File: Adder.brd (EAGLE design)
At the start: 100 x 50 mm, 57 parts, among them U1 LMS8117

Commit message: Updated a few traces
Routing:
- net 3.3V: track 167.7 -> 165.4 mm
- net GND: vias 24 -> 30
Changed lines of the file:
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@@
 <wire x1="2.5" y1="2.25" x2="4" y2="2.25" width="0.1524" layer="1"/>
 <wire x1="1.75" y1="3" x2="2.5" y2="2.25" width="0.1524" layer="1"/>
-<wire x1="1.75" y1="24.25" x2="1.75" y2="10.75" width="0.1524" layer="1"/>
 <wire x1="1.75" y1="10.75" x2="1.75" y2="3" width="0.1524" layer="1"/>
-<wire x1="3.25" y1="24.25" x2="1.75" y2="24.25" width="0.1524" layer="1"/>
 <wire x1="4.75" y1="3" x2="4.95" y2="3" width="0.1524" layer="1"/>
 <wire x1="3.25" y1="24.25" x2="3.225" y2="24.225" width="0.1524" layer="1"/>
@@
 <wire x1="2" y1="11" x2="3.75" y2="11" width="0.1524" layer="16"/>
 <wire x1="2" y1="10.75" x2="2" y2="11" width="0.1524" layer="16"/>
-<wire x1="1.75" y1="10.75" x2="2" y2="10.75" width="0.1524" layer="1"/>
+<wire x1="2" y1="10.75" x2="1.75" y2="10.75" width="0.1524" layer="1"/>
 <wire x1="4.75" y1="12" x2="4.95" y2="12" width="0.1524" layer="1"/>
 <wire x1="84.25" y1="25" x2="84.25" y2="15" width="0.1524" layer="1"/>
@@
 <via x="85.5" y="9.5" extent="1-16" drill="0.35"/>
 <via x="18.5" y="47" extent="1-16" drill="0.35"/>
+<wire x1="3.225" y1="24.225" x2="2.225" y2="24.225" width="0.1524" layer="1"/>
+<wire x1="1.5" y1="23.5" x2="1.5" y2="11.25" width="0.1524" layer="1"/>
+<wire x1="1.5" y1="11.25" x2="2" y2="10.75" width="0.1524" layer="1"/>
+<wire x1="2.225" y1="24.225" x2="1.5" y2="23.5" width="0.1524" layer="1"/>
+<via x="9.5" y="17" extent="1-16" drill="0.35"/>
+<via x="32" y="12.5" extent="1-16" drill="0.35"/>
+<via x="34.5" y="17" extent="1-16" drill="0.35"/>
+<via x="34.5" y="25" extent="1-16" drill="0.35"/>
+<via x="25.5" y="5" extent="1-16" drill="0.35"/>
+<via x="41.5" y="36.5" extent="1-16" drill="0.35"/>
 </signal>
 <signal name="3.3V">
@@
 <wire x1="7.00921875" y1="44.85" x2="7.37" y2="44.85" width="0.6096" layer="1"/>
 <wire x1="7.37" y1="44.85" x2="9.3" y2="46.78" width="0.6096" layer="1"/>
-<wire x1="9.3" y1="42.55921875" x2="9.3" y2="40.48" width="0.6096" layer="1"/>
+<wire x1="9.3" y1="40.607309375" x2="9.3" y2="42.55921875" width="0.6096" layer="1"/>
+<wire x1="9.3" y1="40.607309375" x2="9.3" y2="40.48" width="0.6096" layer="1"/>
 <wire x1="9.3" y1="42.55921875" x2="7.00921875" y2="44.85" width="0.6096" layer="1"/>
 <wire x1="9.3" y1="40.48" x2="9.3" y2="39.7" width="0.6096" layer="1"/>
@@
 <wire x1="63.81" y1="18.54" x2="63.81" y2="16" width="0.6096" layer="1"/>
 <wire x1="63.81" y1="16" x2="63.81" y2="13.46" width="0.6096" layer="1"/>
-<wire x1="3.13" y1="27.9" x2="7.9" y2="27.9" width="0.2" layer="1"/>
+<wire x1="7.9" y1="27.9" x2="3.13" y2="27.9" width="0.2" layer="1"/>
 <wire x1="7.9" y1="27.9" x2="11" y2="31" width="0.2" layer="1"/>
 <wire x1="11" y1="31" x2="12.255" y2="31" width="0.2" layer="1"/>
 <wire x1="12.255" y1="31" x2="12.35" y2="31.095" width="0.2" layer="1"/>
-<wire x1="3.25" y1="39.25" x2="3.25" y2="28" width="0.1524" layer="1"/>
-<wire x1="9.5" y1="39.25" x2="3.25" y2="39.25" width="0.1524" layer="1"/>
 <wire x1="3.25" y1="28" x2="3.13" y2="27.9" width="0.1524" layer="1"/>
 <wire x1="9.5" y1="39.25" x2="9.625" y2="39.375" width="0.1524" layer="1"/>
@@
 <wire x1="36.4124625" y1="6.5" x2="37" y2="7.0875375" width="0.254" layer="1"/>
 <wire x1="28.6" y1="6.5" x2="36.4124625" y2="6.5" width="0.254" layer="1"/>
+<wire x1="3.13" y1="27.9" x2="3.13" y2="34.437309375" width="0.1524" layer="1"/>
+<wire x1="3.13" y1="34.437309375" x2="9.3" y2="40.607309375" width="0.1524" layer="1"/>
 </signal>
 <signal name="N$11">
@@
 <contactref element="R13" pad="2"/>
 <wire x1="29.25" y1="46" x2="28.25" y2="45" width="0.1524" layer="1"/>
-<wire x1="36" y1="46" x2="29.25" y2="46" width="0.1524" layer="1"/>
-<wire x1="37" y1="45" x2="36.5" y2="45.5" width="0.1524" layer="1"/>
-<wire x1="36.5" y1="45.5" x2="36" y2="46" width="0.1524" layer="1"/>
+<wire x1="29.25" y1="46" x2="36" y2="46" width="0.1524" layer="1"/>
+<wire x1="37" y1="45" x2="36" y2="46" width="0.1524" layer="1"/>
 <wire x1="28.25" y1="45" x2="28.1" y2="45" width="0.1524" layer="1"/>
 <wire x1="37" y1="45" x2="37.1" y2="45" width="0.1524" layer="1"/>
 <wire x1="43.5" y1="46.5" x2="44.25" y2="45.75" width="0.1524" layer="1"/>
 <wire x1="44.25" y1="45.75" x2="45" y2="45" width="0.1524" layer="1"/>
-<wire x1="37.5" y1="46.5" x2="43.5" y2="46.5" width="0.1524" layer="1"/>
-<wire x1="36.5" y1="45.5" x2="37.5" y2="46.5" width="0.1524" layer="1"/>
 <wire x1="45" y1="45" x2="45.1" y2="45" width="0.1524" layer="1"/>
 <wire x1="44" y1="43.25" x2="56" y2="31.25" width="0.1524" layer="16"/>
@@
 <wire x1="56" y1="31.25" x2="56.19" y2="31.24" width="0.1524" layer="16"/>
 <via x="44" y="45.5" extent="1-16" drill="0.35"/>
+<wire x1="36" y1="46" x2="36.5" y2="46.5" width="0.1524" layer="1"/>
+<wire x1="36.5" y1="46.5" x2="43.5" y2="46.5" width="0.1524" layer="1"/>
 </signal>
 <signal name="B0_IN">

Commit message: Made updates for v2
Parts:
- removed R19, R20, R21, R22: 51, SparkFun-Resistors:0805
- removed R23, R24, R25, R26, R27, R28, R29, R30, R31: 10K, SparkFun-Resistors:0805
- removed U$2, U$3, U$4, U$5, U$6: (no value), GeekAmmo:SOT23-3
- added Q1, Q2, Q3, Q4, Q5: BSS101, transistor-fet:TO92
- R10, R11, R12, R13, R14, R15, R16, R17, R18: value 51 -> 10K
- moved R1 42.7 mm to (23.0, 45.0), turned to 0 degrees
- moved R3 34.4 mm to (23.0, 40.0), turned to 0 degrees
- moved R18 32.2 mm to (34.0, 5.00), turned to 0 degrees
- moved R5 26.6 mm to (23.0, 35.0), turned to 0 degrees
- moved R13 25.5 mm to (34.0, 20.0)
- moved R9 24.7 mm to (23.0, 5.00), turned to 0 degrees
- moved R2 20.9 mm to (23.0, 25.0), turned to 0 degrees
- moved R8 16.2 mm to (23.0, 10.0), turned to 0 degrees
- moved R17 15.5 mm to (34.0, 10.0)
- moved R15 14.6 mm to (34.0, 15.0)
- moved R10 13.0 mm to (34.0, 45.0)
- moved R11 13.0 mm to (34.0, 25.0)
- moved R4 12.5 mm to (23.0, 20.0), turned to 0 degrees
- moved R16 11.7 mm to (34.0, 30.0)
- moved R7 10.8 mm to (23.0, 30.0), turned to 0 degrees
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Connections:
- removed net N$11: R1.1, S0.A
- removed net N$12: R2.1, S1.A
- removed net N$13: R3.1, S2.A
- removed net N$14: R4.1, S3.A
- removed net N$15: COUT.A, R5.1
- removed net N$24: A0.A, R13.1
- removed net N$25: A1.A, R12.1
- removed net N$26: A2.A, R11.1
- removed net N$27: A3.A, R10.1
- removed net N$28: B0.A, R9.1
- removed net N$29: B1.A, R8.1
- removed net N$30: B2.A, R7.1
- removed net N$31: B3.A, R6.1
- net 3.3V: now also COUT.A, S0.A, S1.A, S2.A, S3.A; no longer R1.2, R2.2, R3.2, R4.2, R5.2
- net A0_IN: now also A0.A, R1.2, R10.2; no longer R13.2, R14.2, R23.2
- net A1_IN: now also A1.A, R3.2; no longer R16.2, R25.2
- net A2_IN: now also A2.A, R14.2, R5.2; no longer R11.2, R18.2, R27.2
- net A3_IN: now also A3.A, R16.2, R7.2; no longer R10.2, R20.2, R29.2
- net B0_IN: now also B0.A, R11.2, R2.2; no longer R15.2, R24.2, R9.2
- net B1_IN: now also B1.A, R13.2, R4.2; no longer R17.2, R26.2, R8.2
- net B2_IN: now also B2.A, R15.2, R6.2; no longer R19.2, R28.2, R7.2
- net B3_IN: now also B3.A, R17.2, R8.2; no longer R21.2, R30.2, R6.2
- net CIN: now also R9.2; no longer R22.2
- net COUT: now also Q5.2; no longer U$6.1
- net GND: now also Q1.1, Q2.1, Q3.1, Q4.1, Q5.1, R10.1, R11.1, R12.1, R13.1, R14.1, R15.1, R16.1, R17.1, R18.2; no longer R23.1, R24.1, R25.1, R26.1, R27.1, R28.1, R29.1, R30.1, R31.2, U$2.2, U$3.2, U$4.2, U$5.2, U$6.2
- net N$1: now also Q2.2; no longer U$3.1
- net N$10: now also Q5.3; no longer U$6.3
- net N$2: now also Q3.2; no longer U$4.1
- net N$3: now also Q4.2; no longer U$5.1
- net N$32: now also R1.1; no longer R14.1
- net N$33: now also R2.1; no longer R15.1
- net N$34: now also R3.1; no longer R16.1
- net N$35: now also R4.1; no longer R17.1
- net N$36: now also R5.1; no longer R18.1
- net N$37: now also R6.1; no longer R19.1
- net N$38: now also R7.1; no longer R20.1
- net N$39: now also R8.1; no longer R21.1
- net N$4: now also Q1.2; no longer U$2.1
- net N$40: now also R18.1, R9.1; no longer R22.1, R31.1
- net N$6: now also Q1.3; no longer U$2.3
- net N$7: now also Q2.3; no longer U$3.3
- net N$8: now also Q3.3; no longer U$4.3
- net N$9: now also Q4.3; no longer U$5.3
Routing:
- net GND: track 331.5 -> 0.00 mm, vias 30 -> 0
- net N$12: track 93.7 -> 0.00 mm
- net N$11: track 83.8 -> 0.00 mm, vias 1 -> 0
- net N$15: track 74.0 -> 0.00 mm, vias 2 -> 0
- net N$26: track 73.8 -> 0.00 mm, vias 2 -> 0
- net N$27: track 73.3 -> 0.00 mm, vias 2 -> 0
- net N$6: track 125.7 -> 53.9 mm, vias 1 -> 0
- net N$28: track 71.3 -> 0.00 mm, vias 1 -> 0
- net N$14: track 68.2 -> 0.00 mm, vias 2 -> 0
- net N$13: track 67.5 -> 0.00 mm
- net N$25: track 55.6 -> 0.00 mm
- net N$24: track 55.1 -> 0.00 mm
- net N$29: track 54.3 -> 0.00 mm, vias 2 -> 0
- net N$8: track 116.9 -> 63.8 mm, vias 1 -> 0
- net N$30: track 51.0 -> 0.00 mm, vias 2 -> 0
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
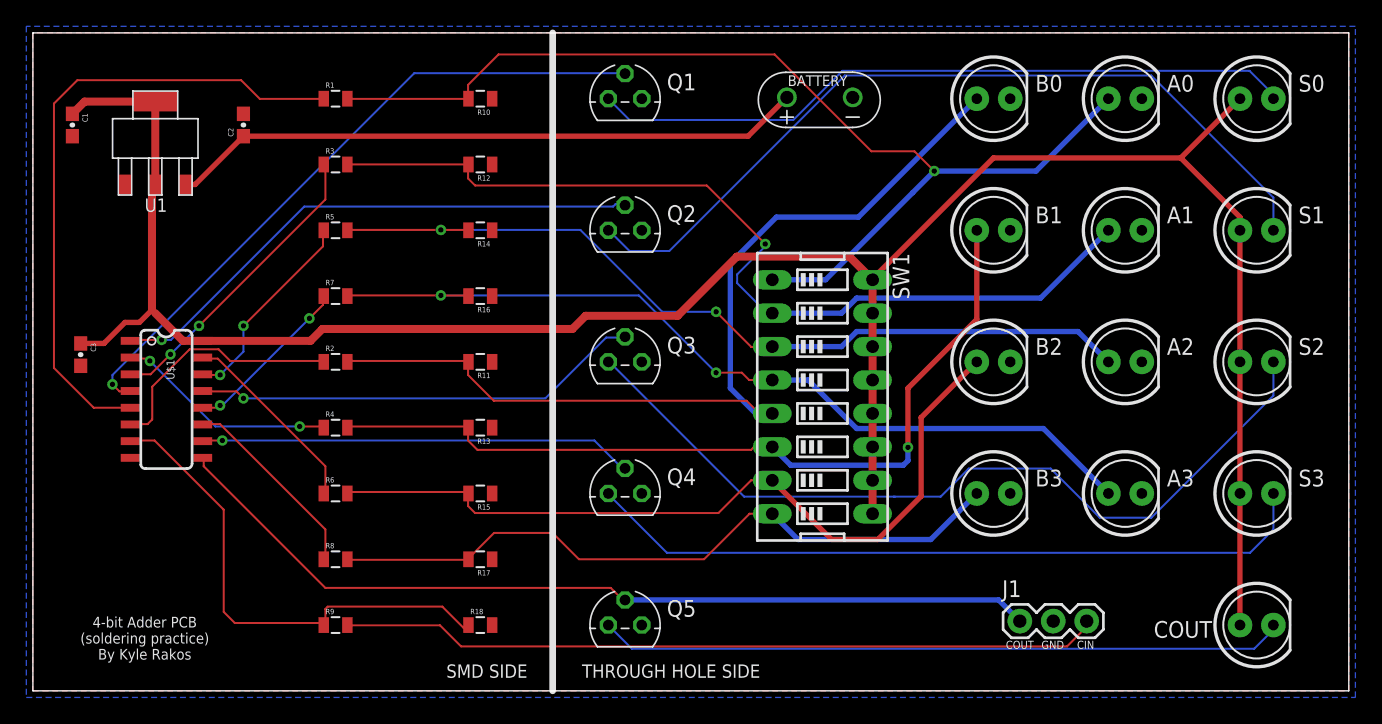
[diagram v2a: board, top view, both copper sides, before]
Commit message: Finished updating v2 of board
Addressed comments in readme and refined layout
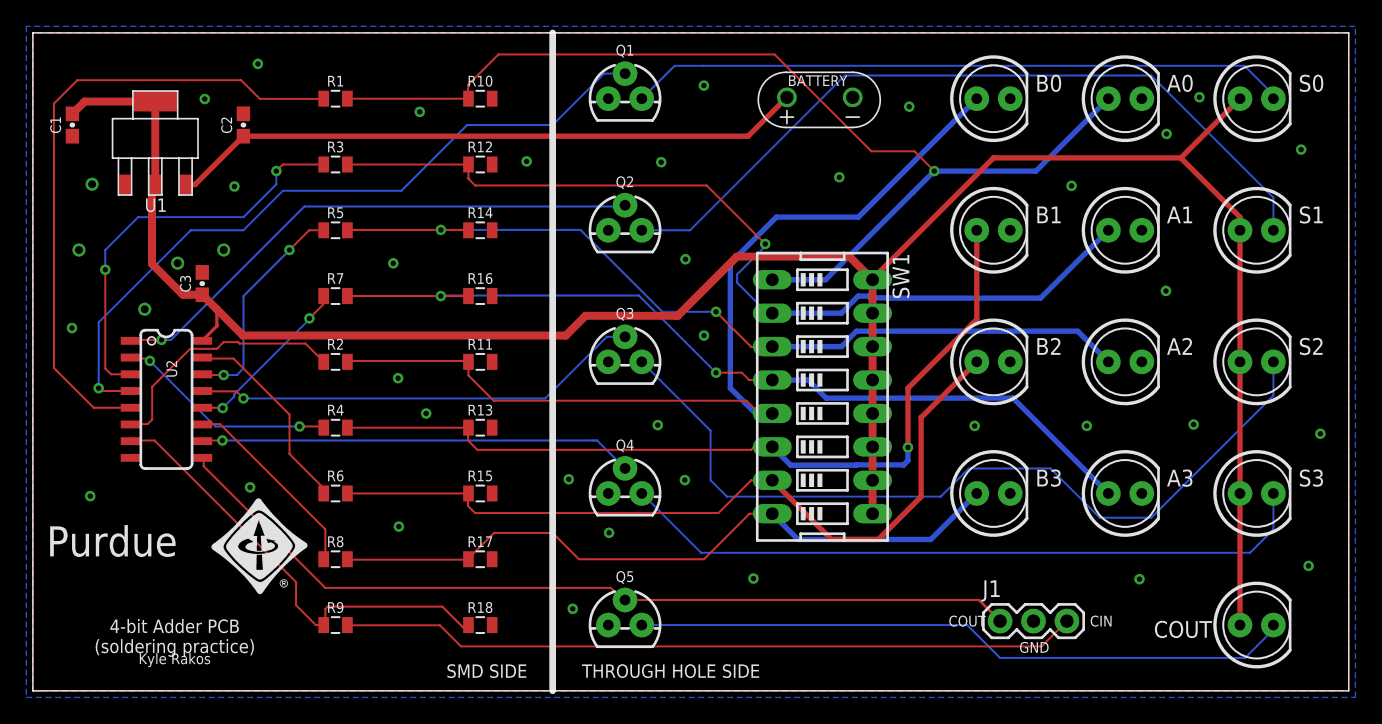
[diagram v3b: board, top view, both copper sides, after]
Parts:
- Q1, Q2, Q3, Q4, Q5: value BSS101 -> MOSFET-NCHANNEL2N7000; device transistor-fet:TO92 -> SparkFun-DiscreteSemi:TO-92
- moved C3 10.7 mm to (12.9, 30.9), turned to 90 degrees
- moved J1 1.50 mm to (73.5, 5.30)
- turned C1 to 90 degrees
- turned R10 to 0 degrees
- turned R11 to 0 degrees
- turned R12 to 0 degrees
- turned R13 to 0 degrees
- turned R14 to 0 degrees
- turned R15 to 0 degrees
- turned R16 to 0 degrees
- turned R17 to 0 degrees
- renumbered U$1 to U2
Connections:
- net 3.3V: now also C1.2; no longer C1.1
- net A0_IN: now also R10.1; no longer R10.2
- net A1_IN: now also R12.1; no longer R12.2
- net A2_IN: now also R14.1; no longer R14.2
- net A3_IN: now also R16.1; no longer R16.2
- net B0_IN: now also R11.1; no longer R11.2
- net B1_IN: now also R13.1; no longer R13.2
- net B2_IN: now also R15.1; no longer R15.2
- net B3_IN: now also R17.1; no longer R17.2
- net GND: now also C1.1, R10.2, R11.2, R12.2, R13.2, R14.2, R15.2, R16.2, R17.2; no longer C1.2, R10.1, R11.1, R12.1, R13.1, R14.1, R15.1, R16.1, R17.1
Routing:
- net N$34: track 23.0 -> 31.3 mm
- net 3.3V: track 177.5 -> 171.5 mm
- net N$4: track 50.8 -> 55.4 mm
- net N$7: track 63.2 -> 59.2 mm
- net N$40: track 38.1 -> 34.5 mm
- net N$6: track 53.9 -> 50.4 mm
- net N$9: track 55.9 -> 53.3 mm
- net N$10: track 52.2 -> 50.3 mm
- net CIN: track 58.1 -> 56.1 mm
- net COUT: track 67.8 -> 66.1 mm
- net N$36: track 15.8 -> 17.2 mm
- net A1_IN: track 72.0 -> 71.0 mm
- net N$37: track 14.9 -> 15.7 mm
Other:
- board text added: "4-bit Adder PCB (soldering practice)"
- board text added: "C:/Users/rakos/Downloads/ieee_mono.bmp"
- board text added: "C:/Users/rakos/Downloads/ieee_mono_logo.bmp"
- board text added: "Kyle Rakos"
- board text added: "Purdue"
- board text removed: "4-bit Adder PCB (soldering practice) By Kyle Rakos"

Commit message: increased minimum trace width
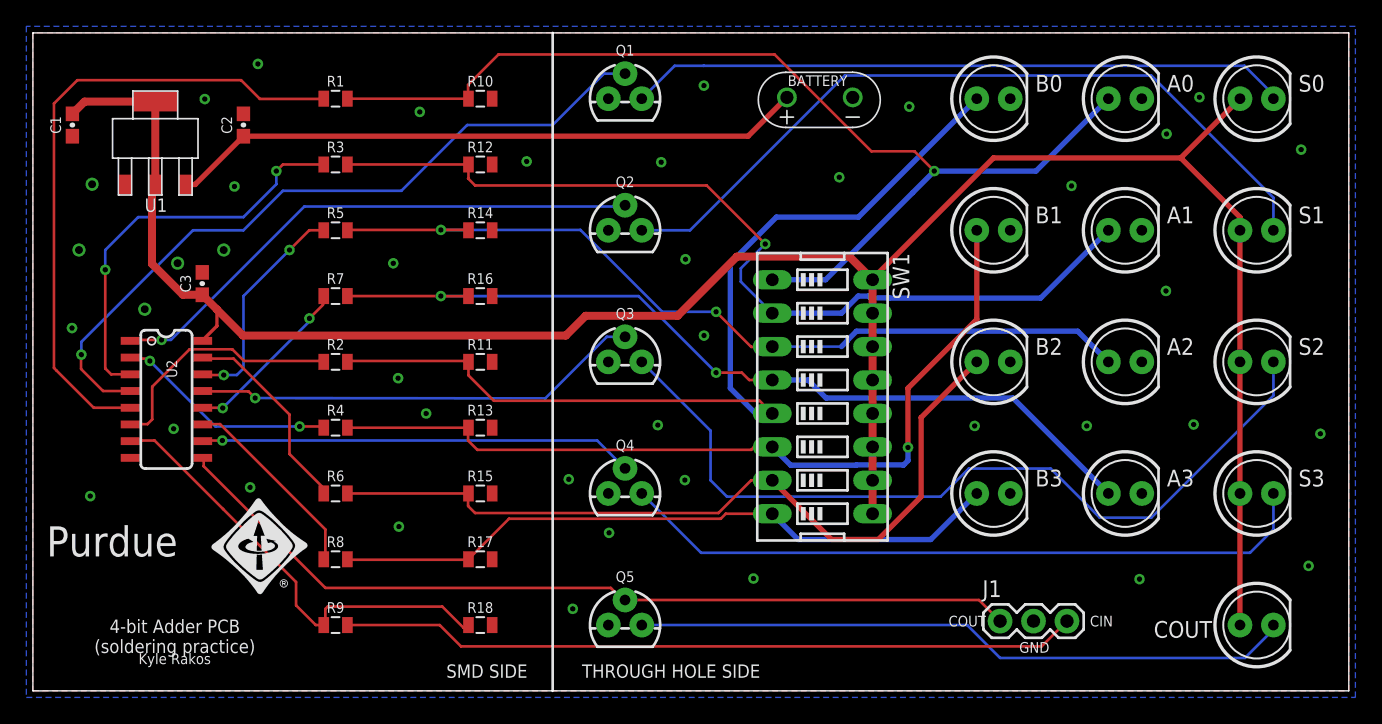
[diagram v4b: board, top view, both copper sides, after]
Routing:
- net B3_IN: track 53.3 -> 51.6 mm
- net N$4: track 55.4 -> 56.3 mm
- net A1_IN: track 71.0 -> 70.3 mm

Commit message: Labels for resistor values
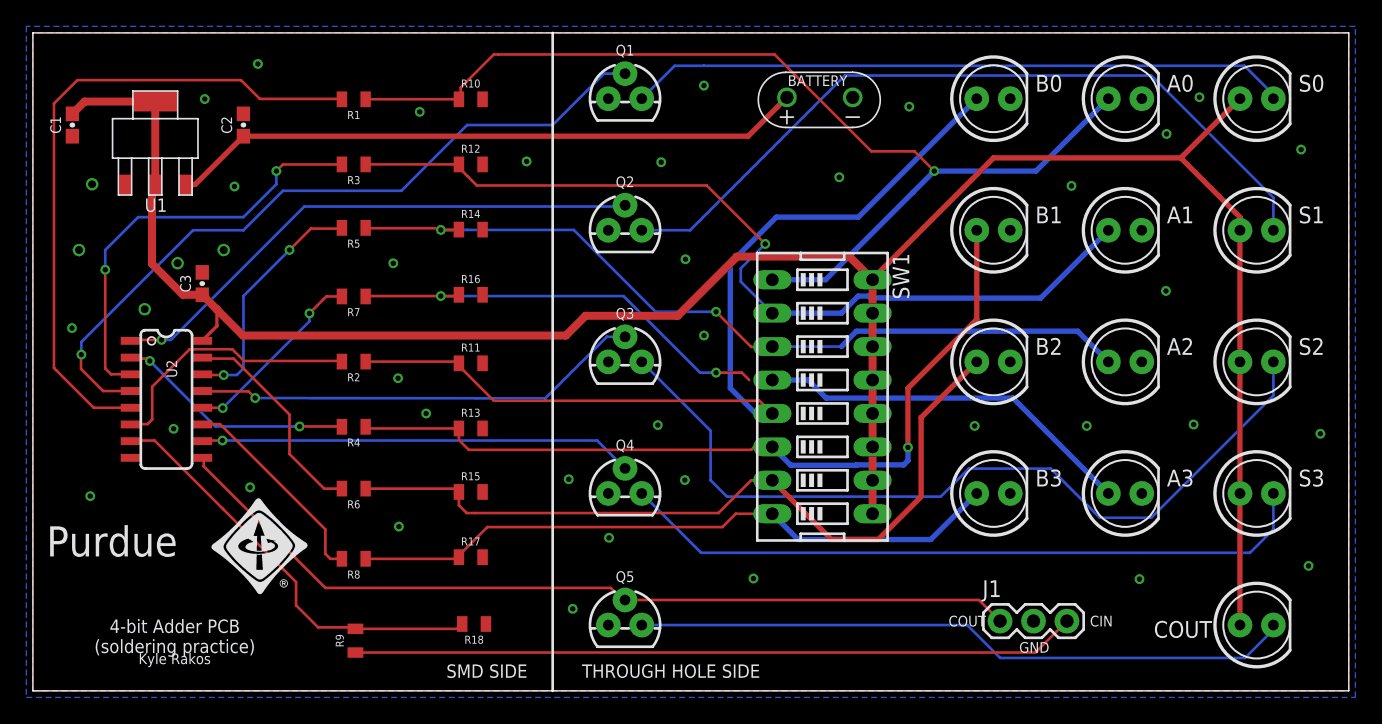
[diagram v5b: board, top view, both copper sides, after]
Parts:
- R10, R11, R12, R13, R14, R15, R16, R17, R18: value 10K -> 10k
- moved R9 1.92 mm to (24.5, 3.81), turned to 90 degrees
- moved R6 1.43 mm to (24.4, 15.4), turned to 180 degrees
- moved R5 1.40 mm to (24.4, 35.2), turned to 180 degrees
- moved R4 1.39 mm to (24.4, 20.1), turned to 180 degrees
- moved R1 1.38 mm to (24.4, 45.0), turned to 180 degrees
- moved R8 1.38 mm to (24.4, 10.0), turned to 180 degrees
- moved R7 1.38 mm to (24.4, 30.0), turned to 180 degrees
- moved R2 1.38 mm to (24.4, 25.0), turned to 180 degrees
- moved R3 1.38 mm to (24.4, 40.0), turned to 180 degrees
- moved R17 0.74 mm to (33.3, 10.2)
- moved R15 0.73 mm to (33.3, 15.1)
- moved R11 0.73 mm to (33.3, 24.9)
- moved R16 0.73 mm to (33.3, 30.1)
- moved R13 0.73 mm to (33.3, 19.9)
- moved R14 0.73 mm to (33.3, 35.1)
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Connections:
- net A0_IN: now also R1.1; no longer R1.2
- net A1_IN: now also R3.1; no longer R3.2
- net A2_IN: now also R5.1; no longer R5.2
- net A3_IN: now also R7.1; no longer R7.2
- net B0_IN: now also R2.1; no longer R2.2
- net B1_IN: now also R4.1; no longer R4.2
- net B2_IN: now also R6.1; no longer R6.2
- net B3_IN: now also R8.1; no longer R8.2
- net CIN: now also R9.1; no longer R9.2
- net GND: now also R18.1; no longer R18.2
- net N$32: now also R1.2; no longer R1.1
- net N$33: now also R2.2; no longer R2.1
- net N$34: now also R3.2; no longer R3.1
- net N$35: now also R4.2; no longer R4.1
- net N$36: now also R5.2; no longer R5.1
- net N$37: now also R6.2; no longer R6.1
- net N$38: now also R7.2; no longer R7.1
- net N$39: now also R8.2; no longer R8.1
- net N$40: now also R18.2, R9.2; no longer R18.1, R9.1
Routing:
- net A3_IN: track 67.6 -> 62.3 mm
- net N$40: track 34.5 -> 32.3 mm
- net A2_IN: track 65.1 -> 63.1 mm
- net A1_IN: track 70.3 -> 68.3 mm
- net B0_IN: track 72.0 -> 70.2 mm
- net B1_IN: track 64.8 -> 63.2 mm
- net A0_IN: track 81.6 -> 80.0 mm
- net N$36: track 17.2 -> 18.6 mm
- net B3_IN: track 51.6 -> 50.2 mm
- net B2_IN: track 61.2 -> 59.8 mm
- net N$32: track 49.0 -> 50.4 mm
- net N$33: track 18.9 -> 20.2 mm
- net N$35: track 16.9 -> 18.2 mm
- net N$38: track 13.3 -> 14.5 mm
- net CIN: track 56.3 -> 55.1 mm
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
